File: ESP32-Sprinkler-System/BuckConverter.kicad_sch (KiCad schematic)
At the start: 13 parts, among them U301 TPS5450DDAR

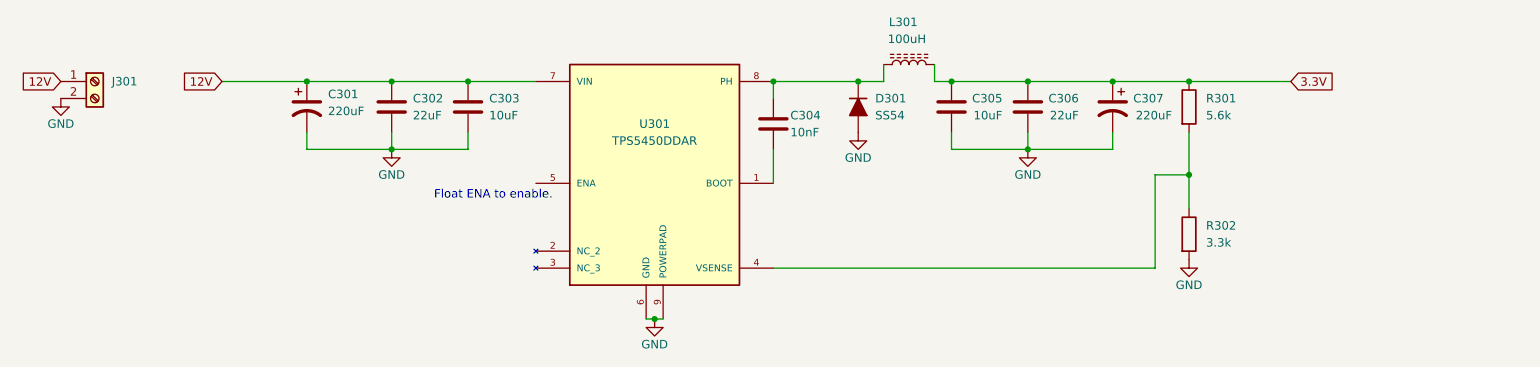
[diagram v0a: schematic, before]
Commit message: Change of plans
We had a change of plans. Rather than having everything made of surface-mount parts, we opted for a simpler through-hole project that could be breadboarded first. This circuit will be revisited and updated when the prototype is complete.
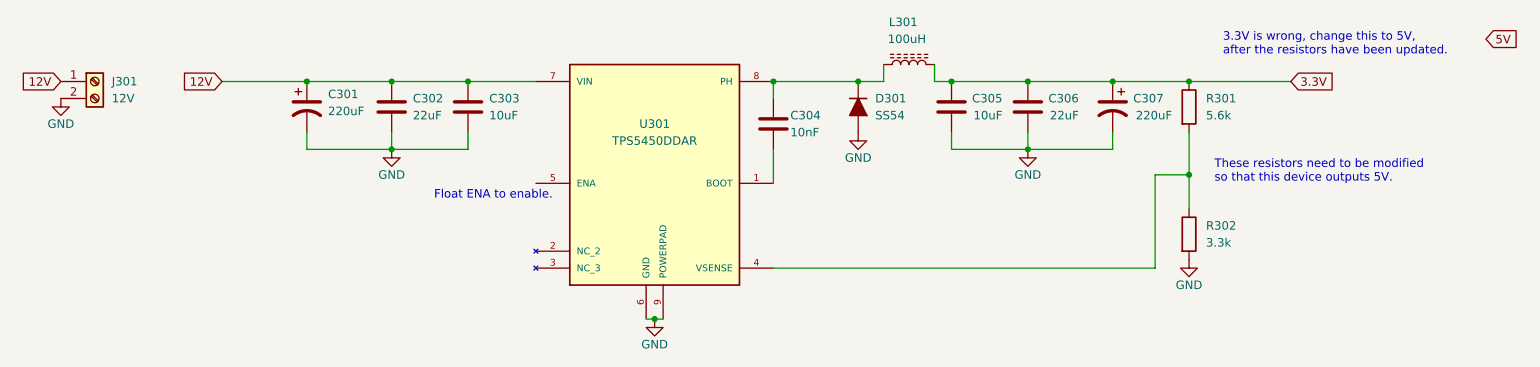
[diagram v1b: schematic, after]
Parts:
- J301: value (none) -> 12V
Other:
- note added: "3.3V is wrong, change this to 5V, after the resistors have been updated."
- note added: "These resistors need to be modified so that this device outputs 5V."
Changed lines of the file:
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@@
     (stroke (width 0) (type default) (color 0 0 0 0))
   )
+  (text "3.3V is wrong, change this to 5V,\nafter the resistors have been updated."
+    (at 223.52 68.58 0)
+    (effects (font (size 1.27 1.27)) (justify left bottom))
+  )
   (text "Float ENA to enable.\n" (at 105.41 90.17 0)
+    (effects (font (size 1.27 1.27)) (justify left bottom))
+  )
+  (text "These resistors need to be modified\nso that this device outputs 5V."
+    (at 222.25 87.63 0)
     (effects (font (size 1.27 1.27)) (justify left bottom))
   )
@@
     )
   )
+  (global_label "5V" (shape input) (at 262.89 66.04 0) (fields_autoplaced)
+    (effects (font (size 1.27 1.27)) (justify left))
+    (property "Intersheet References" "${INTERSHEET_REFS}" (id 0) (at 267.6012 65.9606 0)
+      (effects (font (size 1.27 1.27)) (justify left) hide)
+    )
+  )
   (global_label "12V" (shape input) (at 73.66 72.39 180) (fields_autoplaced)
     (effects (font (size 1.27 1.27)) (justify right))
@@
       (effects (font (size 1.27 1.27)) (justify left))
     )
-    (property "Value" "" (id 1) (at 57.15 74.9299 0)
-      (effects (font (size 1.27 1.27)) (justify left))
-    )
+    (property "Value" "12V" (id 1) (at 57.15 74.9299 0)
+      (effects (font (size 1.27 1.27)) (justify left))
+    )
